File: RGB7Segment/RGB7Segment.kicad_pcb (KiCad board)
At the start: 2 copper layers, 30 parts, among them J1 Conn_01x02_Socket, J2 Conn_01x04_Pin

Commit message: Potential working sol'n for horizontal
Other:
- board outline added: 35.2 x 11.7 mm
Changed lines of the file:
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@@
 			(type default)
 		)
-		(layer "Eco2.User")
+		(layer "Edge.Cuts")
 	)
 	(gr_line
@@
 			(type default)
 		)
-		(layer "Eco2.User")
+		(layer "Edge.Cuts")
 	)
 	(gr_line
@@
 			(type default)
 		)
-		(layer "Eco2.User")
+		(layer "Edge.Cuts")
 	)
 	(gr_line
@@
 			(type default)
 		)
-		(layer "Eco2.User")
+		(layer "Edge.Cuts")
 	)
 	(gr_line
@@
 			(type default)
 		)
-		(layer "Eco2.User")
+		(layer "Edge.Cuts")
 	)
 	(gr_line
@@
 			(type default)
 		)
-		(layer "Eco2.User")
+		(layer "Edge.Cuts")
 	)
 	(gr_line
@@
 			(type default)
 		)
-		(layer "Eco2.User")
+		(layer "Edge.Cuts")
 	)
 	(gr_line
@@
 			(type default)
 		)
-		(layer "Eco2.User")
+		(layer "Edge.Cuts")
 	)
 	(segment
@@
 	(via
 		(at 242.339411 105.791)
-		(size 0.127)
+		(size 0.381)
 		(drill 0.254)
 		(layers "F.Cu" "B.Cu")
@@
 	(via
 		(at 232.278822 104.14)
-		(size 0.127)
+		(size 0.381)
 		(drill 0.254)
 		(layers "F.Cu" "B.Cu")
@@
 	(via
 		(at 226.460589 110.871)
-		(size 0.127)
+		(size 0.381)
 		(drill 0.254)
 		(layers "F.Cu" "B.Cu")
@@
 	(via
 		(at 231.460589 108.712)
-		(size 0.127)
+		(size 0.381)
 		(drill 0.254)
 		(layers "F.Cu" "B.Cu")
@@
 	(via
 		(at 221.336152 108.433152)
-		(size 0.127)
+		(size 0.381)
 		(drill 0.254)
 		(layers "F.Cu" "B.Cu")
@@
 	(via
 		(at 241.860589 110.998)
-		(size 0.127)
+		(size 0.381)
 		(drill 0.254)
 		(layers "F.Cu" "B.Cu")
@@
 	(via
 		(at 222.139411 104.394)
-		(size 0.127)
+		(size 0.381)
 		(drill 0.254)
 		(layers "F.Cu" "B.Cu")
@@
 	(via
 		(at 247.728 104.472)
-		(size 0.127)
+		(size 0.381)
 		(drill 0.254)
 		(layers "F.Cu" "B.Cu")
@@
 	(via
 		(at 227.139411 105.791)
-		(size 0.127)
+		(size 0.381)
 		(drill 0.254)
 		(layers "F.Cu" "B.Cu")
@@
 	(via
 		(at 242.278822 101.854)
-		(size 0.127)
+		(size 0.381)
 		(drill 0.254)
 		(layers "F.Cu" "B.Cu")
@@
 	(via
 		(at 227.139411 101.6)
-		(size 0.127)
+		(size 0.381)
 		(drill 0.254)
 		(layers "F.Cu" "B.Cu")
@@
 	(via
 		(at 236.721178 108.712)
-		(size 0.127)
+		(size 0.381)
 		(drill 0.254)
 		(layers "F.Cu" "B.Cu")
@@
 	(via
 		(at 247.2635 108.4635)
-		(size 0.127)
+		(size 0.381)
 		(drill 0.254)
 		(layers "F.Cu" "B.Cu")
@@
 	(via
 		(at 237.4 104.14)
-		(size 0.127)
+		(size 0.381)
 		(drill 0.254)
 		(layers "F.Cu" "B.Cu")
@@
 	(via
 		(at 225.806 107.823)
-		(size 0.127)
+		(size 0.381)
 		(drill 0.254)
 		(layers "F.Cu" "B.Cu")
@@
 	(via
 		(at 232.283 111.252)
-		(size 0.127)
+		(size 0.381)
 		(drill 0.254)
 		(layers "F.Cu" "B.Cu")
@@
 	(via
 		(at 233.172 102.616)
-		(size 0.127)
+		(size 0.381)
 		(drill 0.254)
 		(layers "F.Cu" "B.Cu")
@@
 	(via
 		(at 236.474 101.727)
-		(size 0.127)
+		(size 0.381)
 		(drill 0.254)
 		(layers "F.Cu" "B.Cu")
@@
 	(via
 		(at 222.377 106.807)
-		(size 0.127)
+		(size 0.381)
 		(drill 0.254)
 		(layers "F.Cu" "B.Cu")
@@
 	(via
 		(at 231.267 101.727)
-		(size 0.127)
+		(size 0.381)
 		(drill 0.254)
 		(layers "F.Cu" "B.Cu")
@@
 	(via
 		(at 231.267 102.616)
-		(size 0.127)
+		(size 0.381)
 		(drill 0.254)
 		(layers "F.Cu" "B.Cu")
@@
 	(via
 		(at 237.998 106.802)
-		(size 0.127)
+		(size 0.381)
 		(drill 0.254)
 		(layers "F.Cu" "B.Cu")
@@
 	(via
 		(at 236.474 102.743)
-		(size 0.127)
+		(size 0.381)
 		(drill 0.254)
 		(layers "F.Cu" "B.Cu")
@@
 	(via
 		(at 230.632 111.125)
-		(size 0.127)
+		(size 0.381)
 		(drill 0.254)
 		(layers "F.Cu" "B.Cu")
@@
 	(via
 		(at 241.046 107.823)
-		(size 0.127)
+		(size 0.381)
 		(drill 0.254)
 		(layers "F.Cu" "B.Cu")
@@
 	(via
 		(at 233.172 101.727)
-		(size 0.127)
+		(size 0.381)
 		(drill 0.254)
 		(layers "F.Cu" "B.Cu")
@@
 	(via
 		(at 235.839 111.125)
-		(size 0.127)
+		(size 0.381)
 		(drill 0.254)
 		(layers "F.Cu" "B.Cu")
@@
 	(via
 		(at 237.617 110.236)
-		(size 0.127)
+		(size 0.381)
 		(drill 0.254)
 		(layers "F.Cu" "B.Cu")
@@
 	(via
 		(at 236.721178 106.045)
-		(size 0.127)
+		(size 0.381)
 		(drill 0.254)
 		(layers "F.Cu" "B.Cu")
@@
 	(via
 		(at 230.886 106.172)
-		(size 0.127)
+		(size 0.381)
 		(drill 0.254)
 		(layers "F.Cu" "B.Cu")
@@
 	(via
 		(at 232.283 110.49)
-		(size 0.127)
+		(size 0.381)
 		(drill 0.254)
 		(layers "F.Cu" "B.Cu")
@@
 	(via
 		(at 247.478822 106.934)
-		(size 0.127)
+		(size 0.381)
 		(drill 0.254)
 		(layers "F.Cu" "B.Cu")
@@
 	(via
 		(at 240.919 103.886)
-		(size 0.127)
+		(size 0.381)
 		(drill 0.254)
 		(layers "F.Cu" "B.Cu")
@@
 	(via
 		(at 232.537 106.863)
-		(size 0.127)
+		(size 0.381)
 		(drill 0.254)
 		(layers "F.Cu" "B.Cu")
@@
 	(via
 		(at 238.252 101.6)
-		(size 0.127)
+		(size 0.381)
 		(drill 0.254)
 		(layers "F.Cu" "B.Cu")
@@
 	(via
 		(at 221.460589 106.172)
-		(size 0.127)
+		(size 0.381)
 		(drill 0.254)
 		(layers "F.Cu" "B.Cu")
@@
 	(via
 		(at 242.951 109.093)
-		(size 0.127)
+		(size 0.381)
 		(drill 0.254)
 		(layers "F.Cu" "B.Cu")
@@
 	(via
 		(at 230.632 110.49)
-		(size 0.127)
+		(size 0.381)
 		(drill 0.254)
 		(layers "F.Cu" "B.Cu")
@@
 	(via
 		(at 235.839 110.236)
-		(size 0.127)
+		(size 0.381)
 		(drill 0.254)
 		(layers "F.Cu" "B.Cu")
@@
 	(via
 		(at 237.617 111.125)
-		(size 0.127)
+		(size 0.381)
 		(drill 0.254)
 		(layers "F.Cu" "B.Cu")
@@
 	(via
 		(at 227.584 109.093)
-		(size 0.127)
+		(size 0.381)
 		(drill 0.254)
 		(layers "F.Cu" "B.Cu")
@@
 	(via
 		(at 238.252 102.87)
-		(size 0.127)
+		(size 0.381)
 		(drill 0.254)
 		(layers "F.Cu" "B.Cu")
@@
 	(via
 		(at 246.660589 106.299)
-		(size 0.127)
+		(size 0.381)
 		(drill 0.254)
 		(layers "F.Cu" "B.Cu")
@@
 	(via
 		(at 225.933 103.759)
-		(size 0.127)
-		(drill 0.254)
-		(layers "F.Cu" "B.Cu")
+		(size 0.381)
+		(drill 0.254)
+		(layers "F.Cu" "B.Cu")

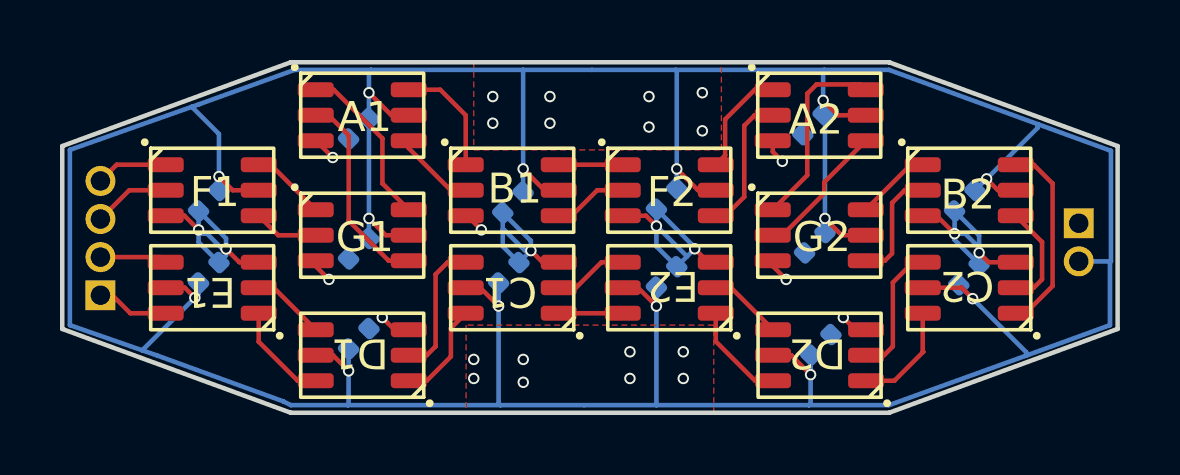
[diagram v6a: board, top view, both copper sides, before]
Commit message: Slightly better spaced layout
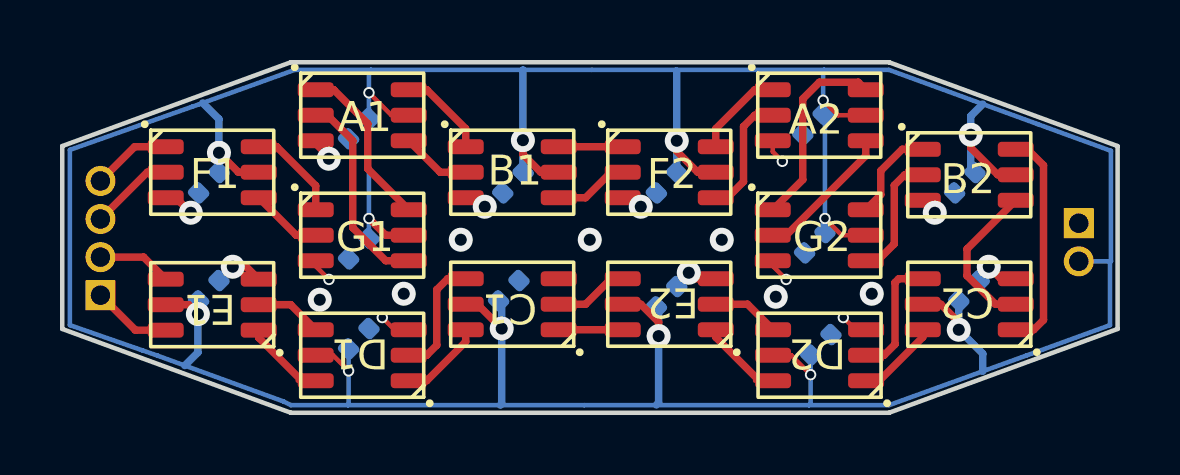
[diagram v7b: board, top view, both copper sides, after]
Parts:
- moved C16 0.66 mm to (237.1, 108.4)
- moved C21 0.66 mm to (231.9, 104.6)
- moved C10 0.60 mm to (221.8, 104.6)
- moved C11 0.60 mm to (221.8, 108.2)
- moved C17 0.60 mm to (231.8, 108.2)
- moved C19 0.60 mm to (247.0, 104.6)
- moved B1 0.60 mm to (230.4, 103.4)
- moved F1 0.60 mm to (220.4, 103.4)
- moved F2 0.60 mm to (235.6, 103.4)
- moved E1 0.56 mm to (223.5, 109.5)
- moved C1 0.55 mm to (233.5, 109.5)
- moved C2 0.55 mm to (248.7, 109.5)
- moved E2 0.55 mm to (238.7, 109.5)
- moved C22 0.54 mm to (237.1, 104.6)
- moved C23 0.54 mm to (247.1, 108.2)
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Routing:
- net GND: track 36.7 -> 12.0 mm, vias 30 -> 20
- net VCC: track 148.3 -> 145.8 mm
- net /B2_CO: track 3.48 -> 5.21 mm
- net /A1_DO: track 3.90 -> 3.04 mm
- net /C2_DO: track 3.60 -> 2.74 mm
- net /B2_DO: track 6.51 -> 7.36 mm
- net /F1_DO: track 2.52 -> 3.24 mm
- net /G2_DO: track 2.52 -> 3.20 mm
- net /DOUT: track 2.42 -> 3.05 mm
- net /F2_DO: track 3.64 -> 3.04 mm
- net /F2_CO: track 4.68 -> 4.12 mm
- net /C1_DO: track 3.39 -> 2.84 mm
- net /C1_CO: track 4.59 -> 4.04 mm
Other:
- board text added: "DIN"
- board text added: "DOUT"
- board text added: "GND"
- board text added: "VCC"

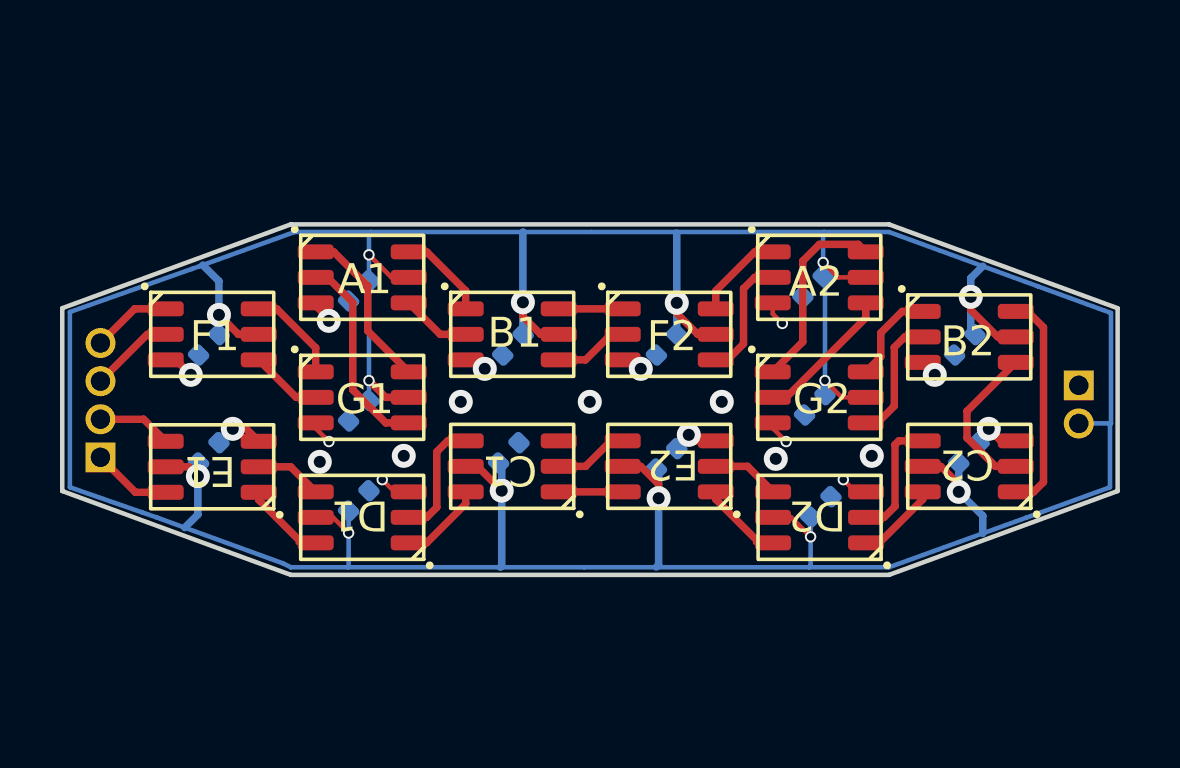
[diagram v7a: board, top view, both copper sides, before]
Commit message: New Layout and placement of parts.
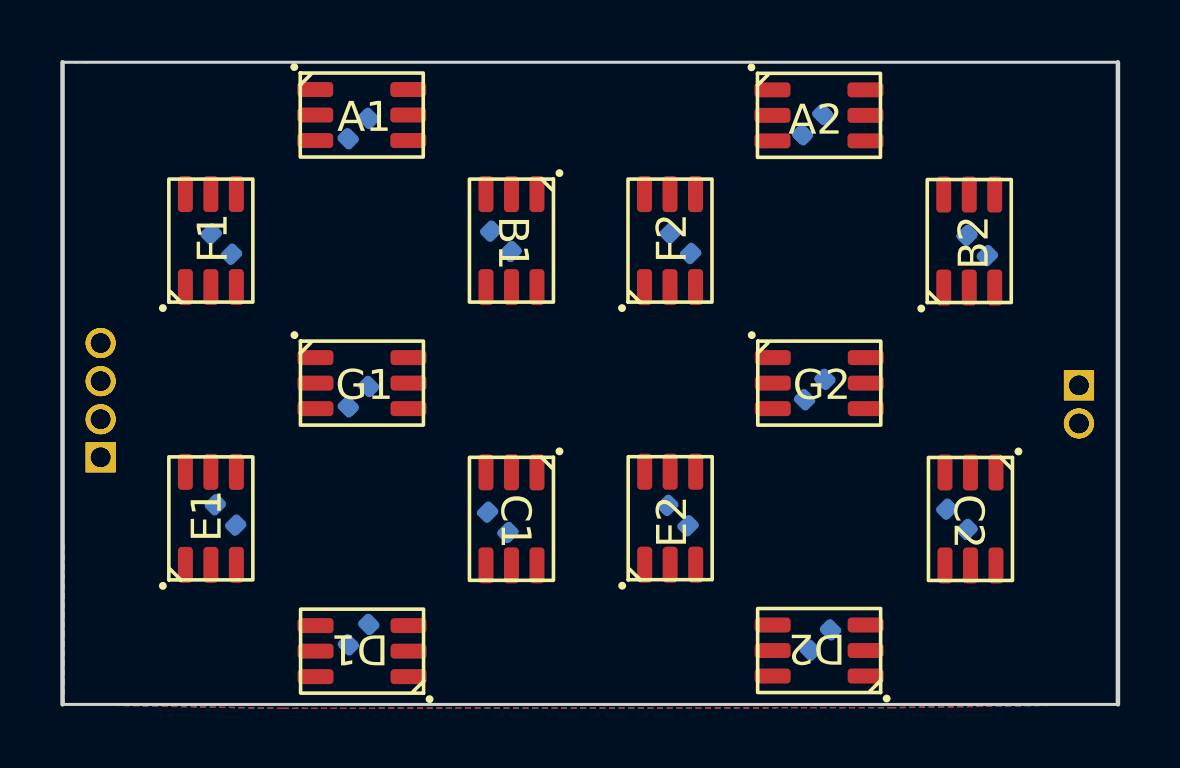
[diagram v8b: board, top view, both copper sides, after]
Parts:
- added J1: Conn_01x02_Socket, Connector_PinHeader_1.27mm:PinHeader_1x02_P1.27mm_Vertical, B.Cu at (250.8, 106.0)
- added J2: Conn_01x04_Pin, Connector_PinHeader_1.27mm:PinHeader_1x04_P1.27mm_Vertical, B.Cu at (218.2, 108.4)
- moved A1 5.41 mm to (225.3, 96.1)
- moved C15 5.41 mm to (226.8, 97.4)
- moved A2 5.40 mm to (240.6, 96.1)
- moved C14 5.40 mm to (241.9, 97.3)
- moved B1 4.50 mm to (232.7, 99.6), turned to -90 degrees
- moved C12 4.46 mm to (226.8, 114.3)
- moved D1 4.46 mm to (228.5, 115.7)
- moved C18 4.44 mm to (242.2, 114.4)
- moved D2 4.44 mm to (243.7, 115.6)
- moved C21 3.47 mm to (231.5, 101.1), turned to 135 degrees
- moved E1 3.44 mm to (221.0, 111.9), turned to 90 degrees
- moved C22 3.42 mm to (237.5, 101.2), turned to -45 degrees
- moved E2 3.39 mm to (236.3, 111.9), turned to 90 degrees
- moved C10 3.39 mm to (222.2, 101.2), turned to -45 degrees
- moved C19 3.34 mm to (247.4, 101.3), turned to -45 degrees
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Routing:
- net VCC: track 145.8 -> 0.00 mm, vias 14 -> 0
- net GND: track 12.0 -> 0.00 mm, vias 20 -> 0
- net /B2_DO: track 7.36 -> 0.00 mm
- net /G1_CO: track 6.81 -> 0.00 mm
- net /A2_DO: track 6.54 -> 0.00 mm
- net /G1_DO: track 5.64 -> 0.00 mm
- net /B2_CO: track 5.21 -> 0.00 mm
- net /A2_CO: track 4.70 -> 0.00 mm
- net /G2_CO: track 4.23 -> 0.00 mm
- net /C2_CO: track 4.15 -> 0.00 mm
- net /F2_CO: track 4.12 -> 0.00 mm
- net /C1_CO: track 4.04 -> 0.00 mm
- net /D2_DO: track 3.36 -> 0.00 mm
- net /D1_DO: track 3.34 -> 0.00 mm
- net /F1_DO: track 3.24 -> 0.00 mm
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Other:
- board size 35.2 x 11.7 mm -> 35.2 x 21.4 mm
